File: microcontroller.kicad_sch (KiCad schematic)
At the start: 27 parts, among them J3 COMM_SELECT, J4 DEBUG_CONN, J5 UART_CONN, J7 UART_SUPP, SW1 BAT_IND, U3 STM32F042F6Px, U5 L78L33_SO8

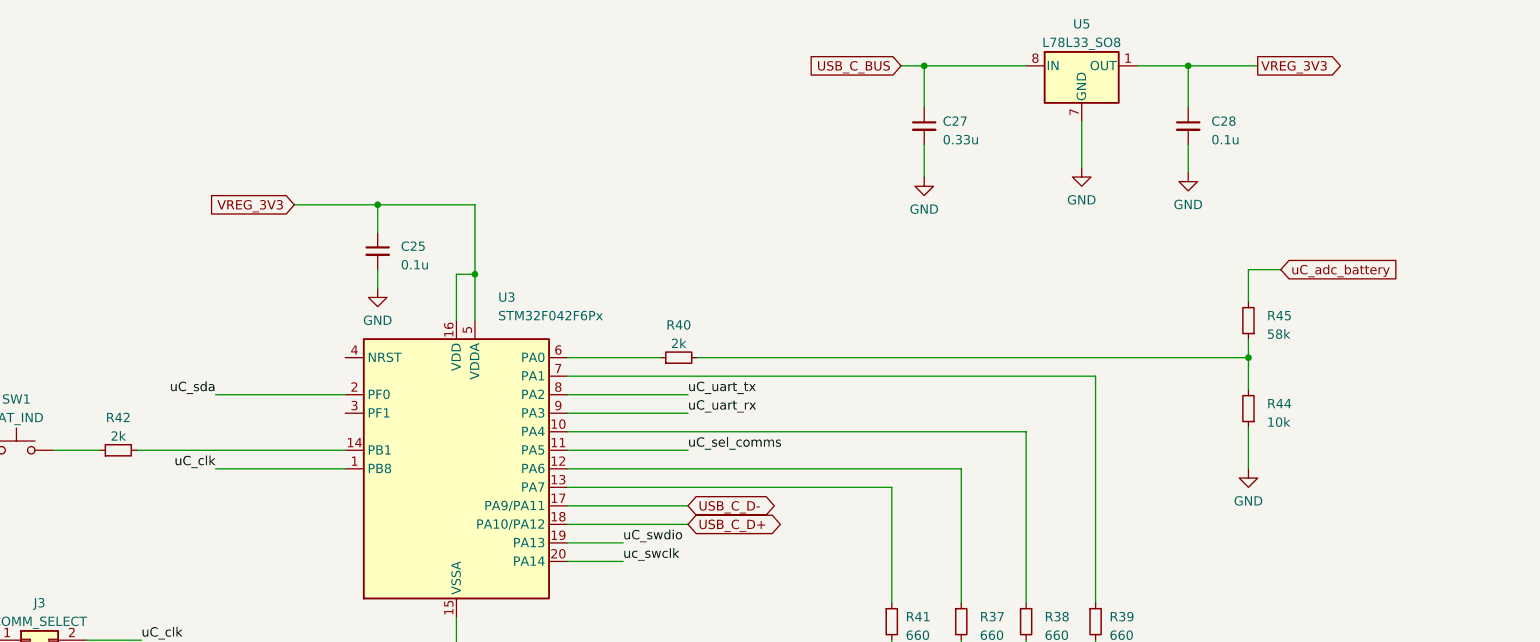
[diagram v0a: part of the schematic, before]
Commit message: Schematic completed. Started routing.
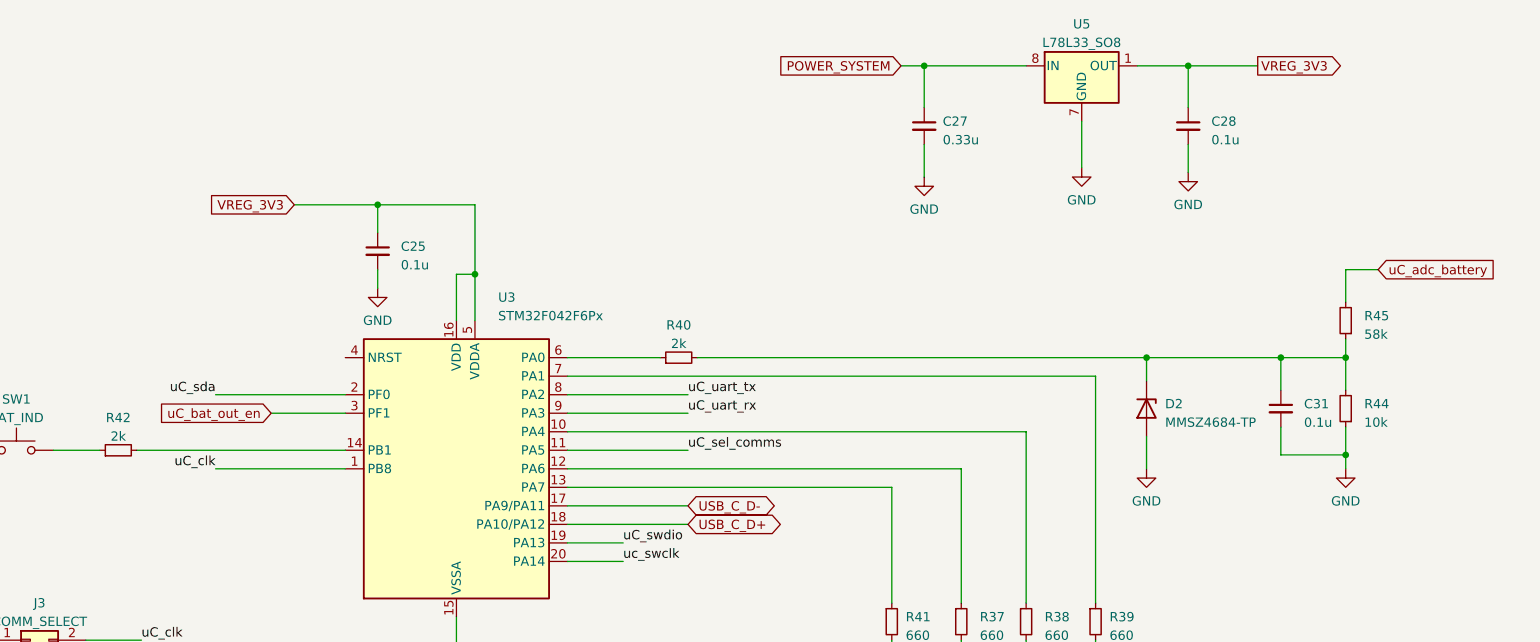
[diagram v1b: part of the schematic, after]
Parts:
- added C31: 0.1u, Capacitor_SMD:C_0805_2012Metric_Pad1.18x1.45mm_HandSolder, symbol Device:C_Small
- added D2: MMSZ4684-TP, Diode_SMD:D_SOD-123, symbol Device:D_Zener
- C25, C27, C28: footprint User_0805:C_0805_2012Metric -> Capacitor_SMD:C_0805_2012Metric_Pad1.18x1.45mm_HandSolder
- D5, D6, D7, D9: footprint User_0805:C_0805_2012Metric -> LED_SMD:LED_0805_2012Metric_Pad1.15x1.40mm_HandSolder
- R37, R38, R39, R40, R41, R42, R43, R44, R45: footprint User_0805:C_0805_2012Metric -> Resistor_SMD:R_0805_2012Metric_Pad1.20x1.40mm_HandSolder
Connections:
- net GND: now also C31.2, D2.2 (A)
- net at R40.2, R44.2, R45.1: now also C31.1, D2.1 (K)
- net uC_bat_out_en: now reaches U3.3 (PF1)
- net USB_C_BUS renamed POWER_SYSTEM
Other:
- moved on the sheet: R44, R45

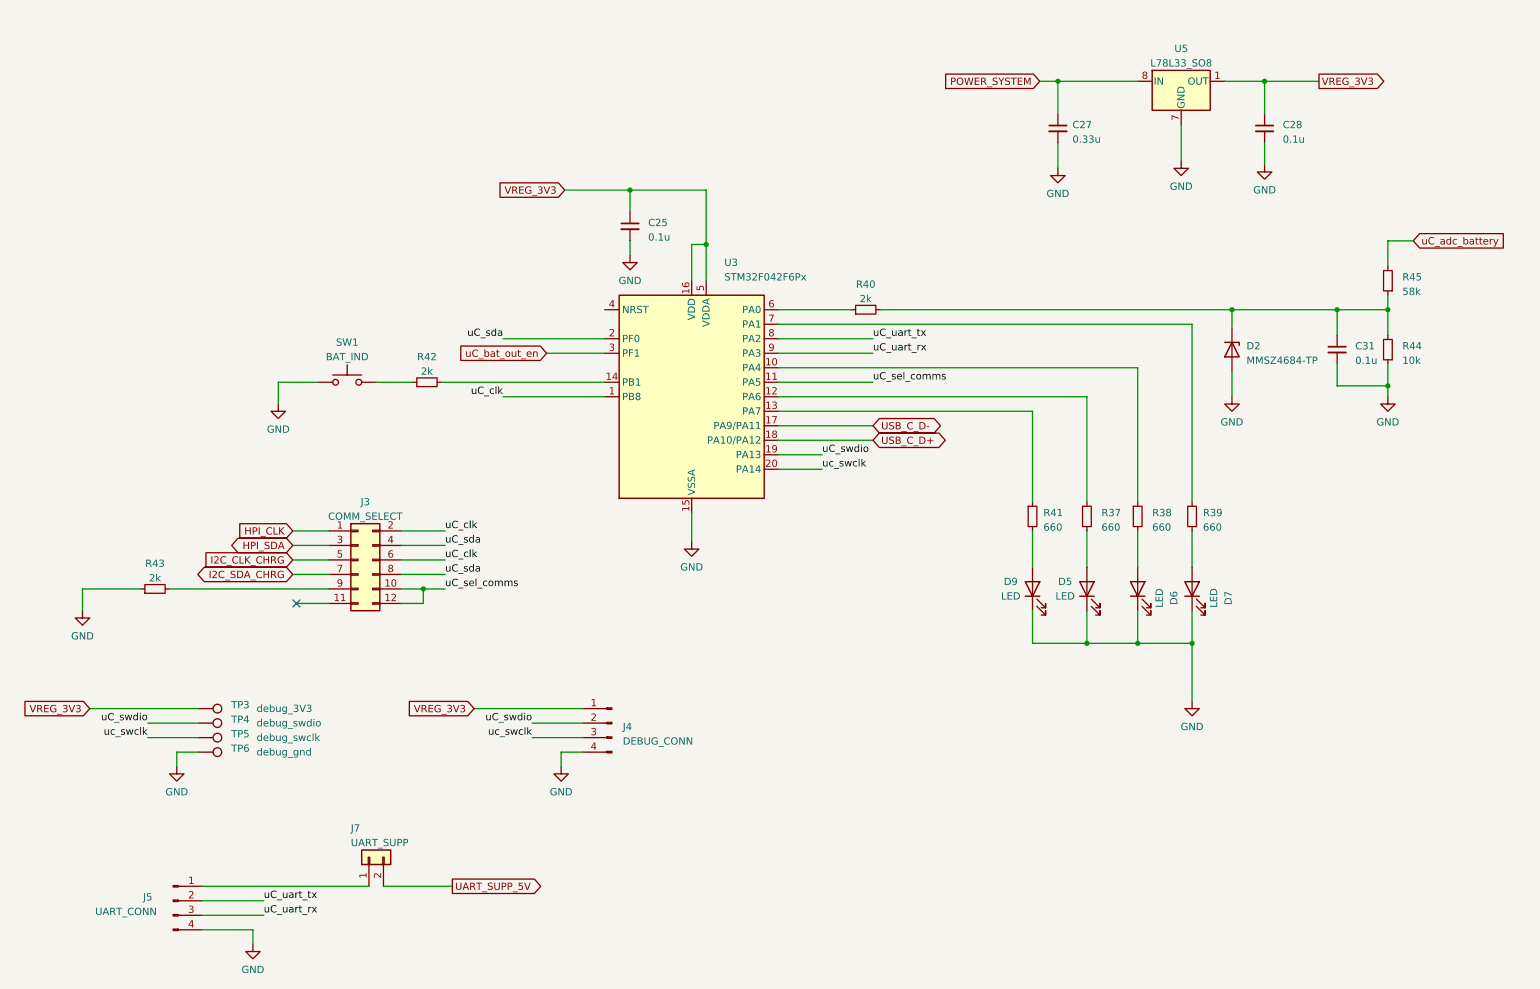
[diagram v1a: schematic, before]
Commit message: Re-reouting the USB C CCX lines
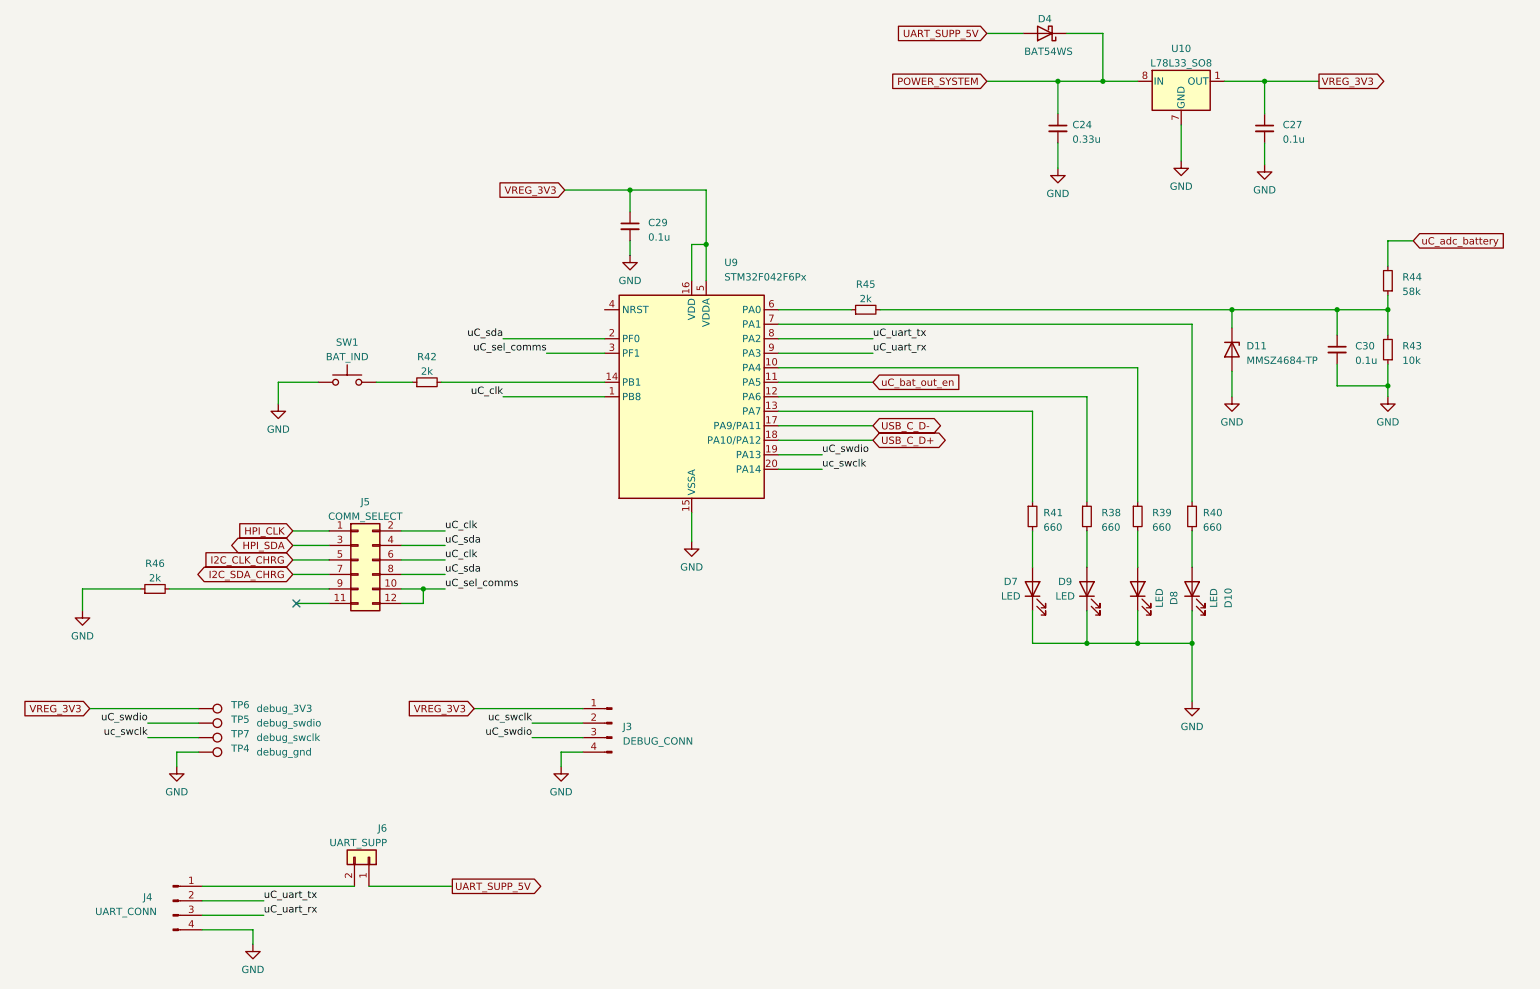
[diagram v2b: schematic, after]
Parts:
- added D4: BAT54WS, Diode_SMD:D_SOD-323_HandSoldering, symbol Device:D_Schottky
- renumbered C27 to C24, C28 to C27, C25 to C29, C31 to C30, D7 to D10, D2 to D11, D9 to D7, D6 to D8, D5 to D9, J4 to J3, J5 to J4, J3 to J5, J7 to J6, R37 to R38, R38 to R39, R39 to R40, R44 to R43, R45 to R44, R40 to R45, R43 to R46, TP6 to TP4, TP4 to TP5, TP3 to TP6, TP5 to TP7, U5 to U10, U3 to U9
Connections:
- net POWER_SYSTEM: now also D4.1 (K)
- net UART_SUPP_5V: now also J6.1 (Pin_1), D4.2 (A); no longer J6.2 (Pin_2)
- net uC_bat_out_en: now also U9.11 (PA5); no longer U9.3 (PF1)
- net uC_sel_comms: now also U9.3 (PF1); no longer U9.11 (PA5)
- net uC_swdio: now also J3.3 (Pin_3); no longer J3.2 (Pin_2)
- net uc_swclk: now also J3.2 (Pin_2); no longer J3.3 (Pin_3)
- net at J4.1 (Pin_1): now also J6.2 (Pin_2); no longer J6.1 (Pin_1)
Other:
- moved on the sheet: J6
